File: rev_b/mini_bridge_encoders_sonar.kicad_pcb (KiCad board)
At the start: 2 copper layers, 33 parts, among them J1 POWER_SELECT, U1 LM2940, U2 LTV-826, U3 LTV-826, U4 LTV-826, U5 754410

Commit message: Added Edge Cuts.
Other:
- board outline added: 50 x 50 mm

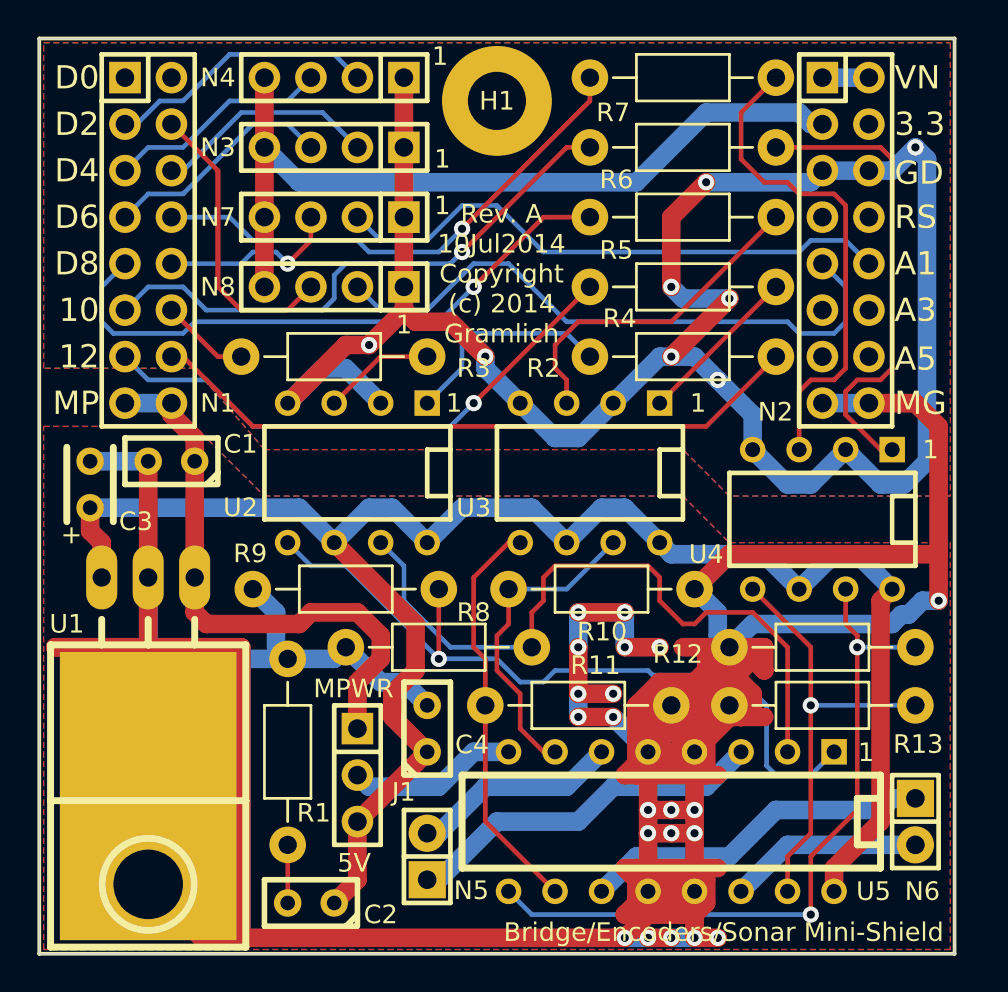
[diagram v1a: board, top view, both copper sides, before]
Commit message: Dealt with some more PCB edge incursions.
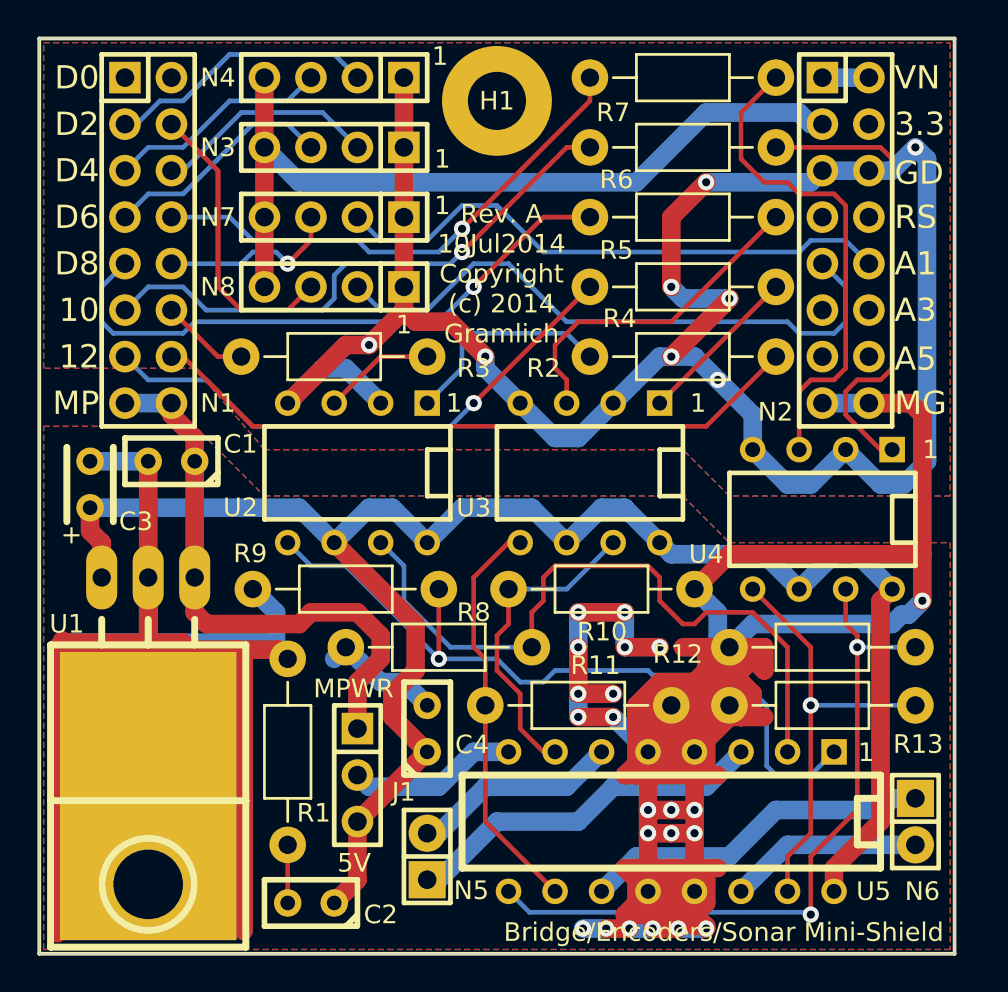
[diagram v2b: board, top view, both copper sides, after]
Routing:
- net /MGND: track 347.7 -> 374.4 mm, vias 21 -> 22
